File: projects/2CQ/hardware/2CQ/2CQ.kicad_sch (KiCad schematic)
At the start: 1 part

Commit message: KiCad Schematic
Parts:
- added DS1: ~, 128x64_0.96_Disp_Module:128x64_0.96_Disp_Module, symbol 2CQ:SSD1306_0.96_128x64_7P
- added EP1: EURORACK_POWERHEADER, symbol ES_Daisy_Patch_SM_FB_Rev1-eagle-import:EURORACK_POWERHEADER
- added J_CV1, J_CV2, J_CV3, J_CV4, J_CV5, J_CV6, J_CV7, J_CV8: EURO_JACK, symbol ES_Daisy_Patch_SM_FB_Rev1-eagle-import:EURO_JACK
- added S1: TAC_SWITCH_PTH, symbol ES_Daisy_Patch_SM_FB_Rev1-eagle-import:TAC_SWITCH_PTH
- added SW1: TOGGLE_ON-ON, symbol ES_Daisy_Patch_SM_FB_Rev1-eagle-import:TOGGLE_ON-ON
- added VR1, VR2, VR3, VR4: M-10K-B-D, ES_Daisy_Patch_SM_FB_Rev1:9MM_SNAP-IN_POT_SILK, symbol ES_Daisy_Patch_SM_FB_Rev1-cache:ES_Daisy_Patch_SM_FB_Rev1-eagle-import_POT_9MM_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
- U1: renamed from 1; footprint (none) -> ES_Daisy_Patch_SM_FB_Rev1:ES_DAISY_PATCH_SM_REV1
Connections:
- net -12V: now reaches U1.A1 (-12V)
- net -12V: now also EP1.-12V0 (-12VIN), EP1.-12V1 (-12VIN)
- net +3V3: now reaches U1.A10 (+3V3)
- net +3V3: now also DS1.2 (VCC)
- net SIG_UART_RX: now reaches U1.A2 (UART_RX)
- net SIG_UART_RX: now also DS1.6 (DC)
- net SIG_UART_TX: now reaches U1.A3 (UART_TX)
- net SIG_UART_TX: now also DS1.5 (RES)
- net GND: now reaches U1.A4 (GND), U1.A7 (GND)
- net GND: now also DS1.1 (GND), EP1.GND0 (GND), EP1.GND1 (GND), EP1.GND2 (GND), EP1.GND3 (GND), EP1.GND4 (GND), EP1.GND5 (GND), J_CV1.GND, J_CV2.GND, J_CV3.GND, J_CV4.GND, J_CV7.GND, J_CV8.GND, S1.3, S1.4, SW1.1 (O), VR1.1, VR2.1, VR3.1, VR4.1
- net +12V: now reaches U1.A5 (+12V)
- net +12V: now also EP1.+12V0 (+12VIN), EP1.+12V1 (+12VIN)
- net +5V: now reaches U1.A6 (+5V)
- net +5V: now also VR1.3, VR2.3, VR3.3, VR4.3
- net SIG_GATE_IN_1: now reaches U1.B10 (GATE_IN_1)
- net SIG_GATE_IN_1: now also J_CV5.TIP
- net SIG_GATE_OUT_1: now reaches U1.B5 (GATE_OUT_1)
- net SIG_GATE_OUT_1: now also J_CV7.TIP
- net SIG_GATE_OUT_2: now reaches U1.B6 (GATE_OUT_2)
- net SIG_GATE_OUT_2: now also J_CV8.TIP
- net SIG_SW_1: now reaches U1.B7 (I2C1_SCL)
- net SIG_SW_1: now also S1.1, S1.2
- net SIG_SW_2: now reaches U1.B8 (I2C1_SDA)
- net SIG_SW_2: now also SW1.2 (P)
- net SIG_GATE_IN_2: now reaches U1.B9 (GATE_IN_2)
- net SIG_GATE_IN_2: now also J_CV6.TIP
- net SIG_CVOUT_2: now reaches U1.C1 (CV_OUT_2)
- net SIG_CVOUT_2: now also J_CV4.TIP
- net SIG_CVOUT_1: now reaches U1.C10 (CV_OUT_1)
- net SIG_CVOUT_1: now also J_CV3.TIP
- net SIG_KNOB4: now reaches U1.C2 (CV4)
- net SIG_KNOB4: now also VR4.2
- net SIG_KNOB3: now reaches U1.C3 (CV3)
- net SIG_KNOB3: now also VR3.2
- net SIG_KNOB2: now reaches U1.C4 (CV2)
- net SIG_KNOB2: now also VR2.2
- net SIG_KNOB1: now reaches U1.C5 (CV1)
- net SIG_KNOB1: now also VR1.2
- net SIG_CV1: now reaches U1.C6 (CV5)
- net SIG_CV1: now also J_CV1.TIP
- net SIG_CV2: now reaches U1.C7 (CV6)
- net SIG_CV2: now also J_CV2.TIP
- net SIG_CV3: now reaches U1.C8 (CV7)
- net SIG_CV4: now reaches U1.C9 (CV8)
- net SIG_SPI_NSS: now reaches U1.D1 (SPI_NSS)
- net SIG_SPI_NSS: now also J_CV5.GND
- net SIG_SPI_SCK: now reaches U1.D10 (SPI_SCK)
- net SIG_SPI_SCK: now also DS1.3 (D0)
- net SD_D3: now reaches U1.D2 (SDMMC_D3)
- net SD_D3: now also J_CV6.GND
- net SD_D2: now reaches U1.D3 (SDMMC_D2)
- net SD_D1: now reaches U1.D4 (SDMMC_D1)
- net SD_D0: now reaches U1.D5 (SDMMC_D0)
- net SD_CK: now reaches U1.D6 (SDMMC_CK)
- net SD_CMD: now reaches U1.D7 (SDMMC_CMD)
- net SIG_SPI_MISO: now reaches U1.D8 (SPI_MISO)
- net SIG_SPI_MOSI: now reaches U1.D9 (SPI_MOSI)
- net SIG_SPI_MOSI: now also DS1.4 (D1)

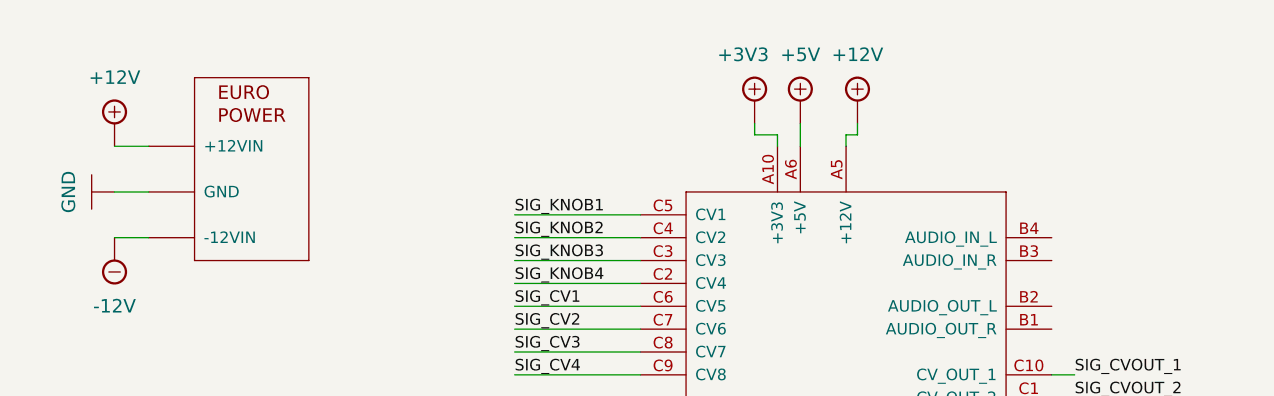
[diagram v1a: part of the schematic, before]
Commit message: Added footprints and some labels
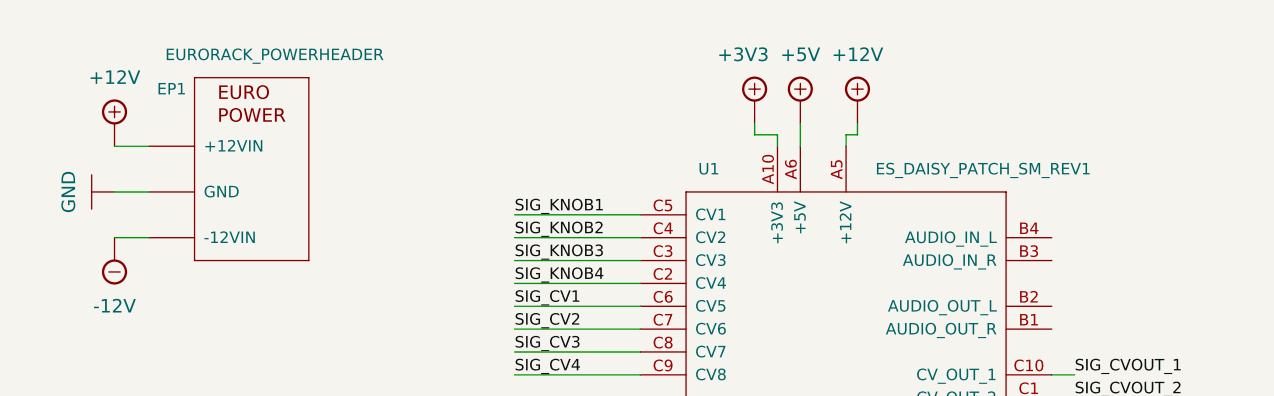
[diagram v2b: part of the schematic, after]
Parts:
- DS1: symbol 2CQ:SSD1306_0.96_128x64_7P -> 2CQ:SSD1306_96_128_64_7P
- EP1: footprint (none) -> ES_Daisy_Patch_SM_FB_Rev1:EURORACK_POWER_SHROUD_LOCK
- J_CV1, J_CV2, J_CV3, J_CV4, J_CV5, J_CV6, J_CV7, J_CV8: footprint (none) -> ES_Daisy_Patch_SM_FB_Rev1:S_JACK
- S1: footprint (none) -> ES_Daisy_Patch_SM_FB_Rev1:TL1105SPF250Q_SILK
- SW1: footprint (none) -> ES_Daisy_Patch_SM_FB_Rev1:TOGGLE_ON-ON
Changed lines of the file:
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@@
   )
   (symbol (lib_id "ES_Daisy_Patch_SM_FB_Rev1-eagle-import:EURORACK_POWERHEADER") (at 36.83 43.18 0) (unit 1)
-    (in_bom yes) (on_board yes) (dnp no) (fields_autoplaced)
-    (property "Reference" "EP1" (at 36.83 43.18 0)
-      (effects (font (size 1.27 1.27)) hide)
-    )
-    (property "Value" "EURORACK_POWERHEADER" (at 36.83 43.18 0)
-      (effects (font (size 1.27 1.27)) hide)
-    )
-    (property "Footprint" "" (at 36.83 43.18 0)
+    (in_bom yes) (on_board yes) (dnp no)
+    (property "Reference" "EP1" (at 29.21 34.29 0)
+      (effects (font (size 1.27 1.27)))
+    )
+    (property "Value" "EURORACK_POWERHEADER" (at 40.64 30.48 0)
+      (effects (font (size 1.27 1.27)))
+    )
+    (property "Footprint" "ES_Daisy_Patch_SM_FB_Rev1:EURORACK_POWER_SHROUD_LOCK" (at 36.83 43.18 0)
       (effects (font (size 1.27 1.27)) hide)
     )
@@
       (effects (font (size 1.4986 1.4986)) (justify left))
     )
-    (property "Footprint" "" (at 66.04 167.64 0)
+    (property "Footprint" "ES_Daisy_Patch_SM_FB_Rev1:S_JACK" (at 66.04 167.64 0)
       (effects (font (size 1.27 1.27)) hide)
     )
@@
       (effects (font (size 1.4986 1.4986)) (justify left))
     )
-    (property "Footprint" "" (at 63.5 124.46 0)
+    (property "Footprint" "ES_Daisy_Patch_SM_FB_Rev1:S_JACK" (at 63.5 124.46 0)
       (effects (font (size 1.27 1.27)) hide)
     )
@@
       (effects (font (size 1.4986 1.4986)))
     )
-    (property "Footprint" "" (at 231.14 90.17 0)
+    (property "Footprint" "ES_Daisy_Patch_SM_FB_Rev1:TOGGLE_ON-ON" (at 231.14 90.17 0)
       (effects (font (size 1.27 1.27)) hide)
     )
@@
       (effects (font (size 1.4986 1.4986)) (justify left))
     )
-    (property "Footprint" "" (at 30.48 124.46 0)
+    (property "Footprint" "ES_Daisy_Patch_SM_FB_Rev1:S_JACK" (at 30.48 124.46 0)
       (effects (font (size 1.27 1.27)) hide)
     )
@@
   )
   (symbol (lib_id "ES_Daisy_Patch_SM_FB_Rev1-eagle-import:ES_DAISY_PATCH_SM_REV1") (at 104.14 73.66 0) (unit 1)
-    (in_bom yes) (on_board yes) (dnp no) (fields_autoplaced)
-    (property "Reference" "U1" (at 104.14 73.66 0)
-      (effects (font (size 1.27 1.27)) hide)
-    )
-    (property "Value" "ES_DAISY_PATCH_SM_REV1" (at 104.14 73.66 0)
-      (effects (font (size 1.27 1.27)) hide)
+    (in_bom yes) (on_board yes) (dnp no)
+    (property "Reference" "U1" (at 88.9 43.18 0)
+      (effects (font (size 1.27 1.27)))
+    )
+    (property "Value" "ES_DAISY_PATCH_SM_REV1" (at 119.38 43.18 0)
+      (effects (font (size 1.27 1.27)))
     )
     (property "Footprint" "ES_Daisy_Patch_SM_FB_Rev1:ES_DAISY_PATCH_SM_REV1" (at 104.14 73.66 0)
@@
       (effects (font (size 1.4986 1.4986)) (justify left))
     )
-    (property "Footprint" "" (at 30.48 144.78 0)
+    (property "Footprint" "ES_Daisy_Patch_SM_FB_Rev1:S_JACK" (at 30.48 144.78 0)
       (effects (font (size 1.27 1.27)) hide)
     )
@@
       (effects (font (size 1.4986 1.4986)) (justify left))
     )
-    (property "Footprint" "" (at 63.5 144.78 0)
+    (property "Footprint" "ES_Daisy_Patch_SM_FB_Rev1:S_JACK" (at 63.5 144.78 0)
       (effects (font (size 1.27 1.27)) hide)
     )
@@
     )
   )
-  (symbol (lib_id "2CQ:SSD1306_0.96_128x64_7P") (at 36.83 78.74 270) (unit 1)
+  (symbol (lib_id "2CQ:SSD1306_96_128_64_7P") (at 36.83 78.74 270) (unit 1)
     (in_bom yes) (on_board yes) (dnp no) (fields_autoplaced)
     (property "Reference" "DS1" (at 26.67 77.47 90)
@@
       (effects (font (size 1.4986 1.4986)) (justify left))
     )
-    (property "Footprint" "" (at 64.77 185.42 0)
+    (property "Footprint" "ES_Daisy_Patch_SM_FB_Rev1:S_JACK" (at 64.77 185.42 0)
       (effects (font (size 1.27 1.27)) hide)
     )
@@
     )
   )
-  (symbol (lib_id "ES_Daisy_Patch_SM_FB_Rev1-eagle-import:EURO_JACK") (at 30.48 166.37 0) (mirror y) (unit 1)
+  (symbol (lib_name "EURO_JACK_1") (lib_id "ES_Daisy_Patch_SM_FB_Rev1-eagle-import:EURO_JACK") (at 30.48 166.37 0) (mirror y) (unit 1)
     (in_bom yes) (on_board yes) (dnp no)
     (property "Reference" "J_CV5" (at 31.75 161.29 0)
@@
       (effects (font (size 1.4986 1.4986)) (justify left))
     )
-    (property "Footprint" "" (at 30.48 166.37 0)
+    (property "Footprint" "ES_Daisy_Patch_SM_FB_Rev1:S_JACK" (at 30.48 166.37 0)
       (effects (font (size 1.27 1.27)) hide)
     )
@@
       (effects (font (size 1.4986 1.4986)) (justify left))
     )
-    (property "Footprint" "" (at 29.21 184.15 0)
+    (property "Footprint" "ES_Daisy_Patch_SM_FB_Rev1:S_JACK" (at 29.21 184.15 0)
       (effects (font (size 1.27 1.27)) hide)
     )
@@
       (effects (font (size 1.4986 1.4986)))
     )
-    (property "Footprint" "" (at 187.96 90.17 0)
-      (effects (font (size 1.27 1.27)) hide)
-    )
+    (property "Footprint" "ES_Daisy_Patch_SM_FB_Rev1:TL1105SPF250Q_SILK" (at 187.96 90.17 0)
+      (effects (font (size 1.27 1.27)) hide)
+    )

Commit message: Use project footprint for 128x64_0.96_Disp_Module
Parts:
- DS1: footprint 128x64_0.96_Disp_Module:128x64_0.96_Disp_Module -> 2CQ:128x64_0.96_Disp_Module
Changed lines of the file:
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@@
       (effects (font (size 1.27 1.27)))
     )
-    (property "Footprint" "128x64_0.96_Disp_Module:128x64_0.96_Disp_Module" (at 36.83 78.74 0)
+    (property "Footprint" "2CQ:128x64_0.96_Disp_Module" (at 36.83 78.74 0)
       (effects (font (size 1.27 1.27)) hide)
     )

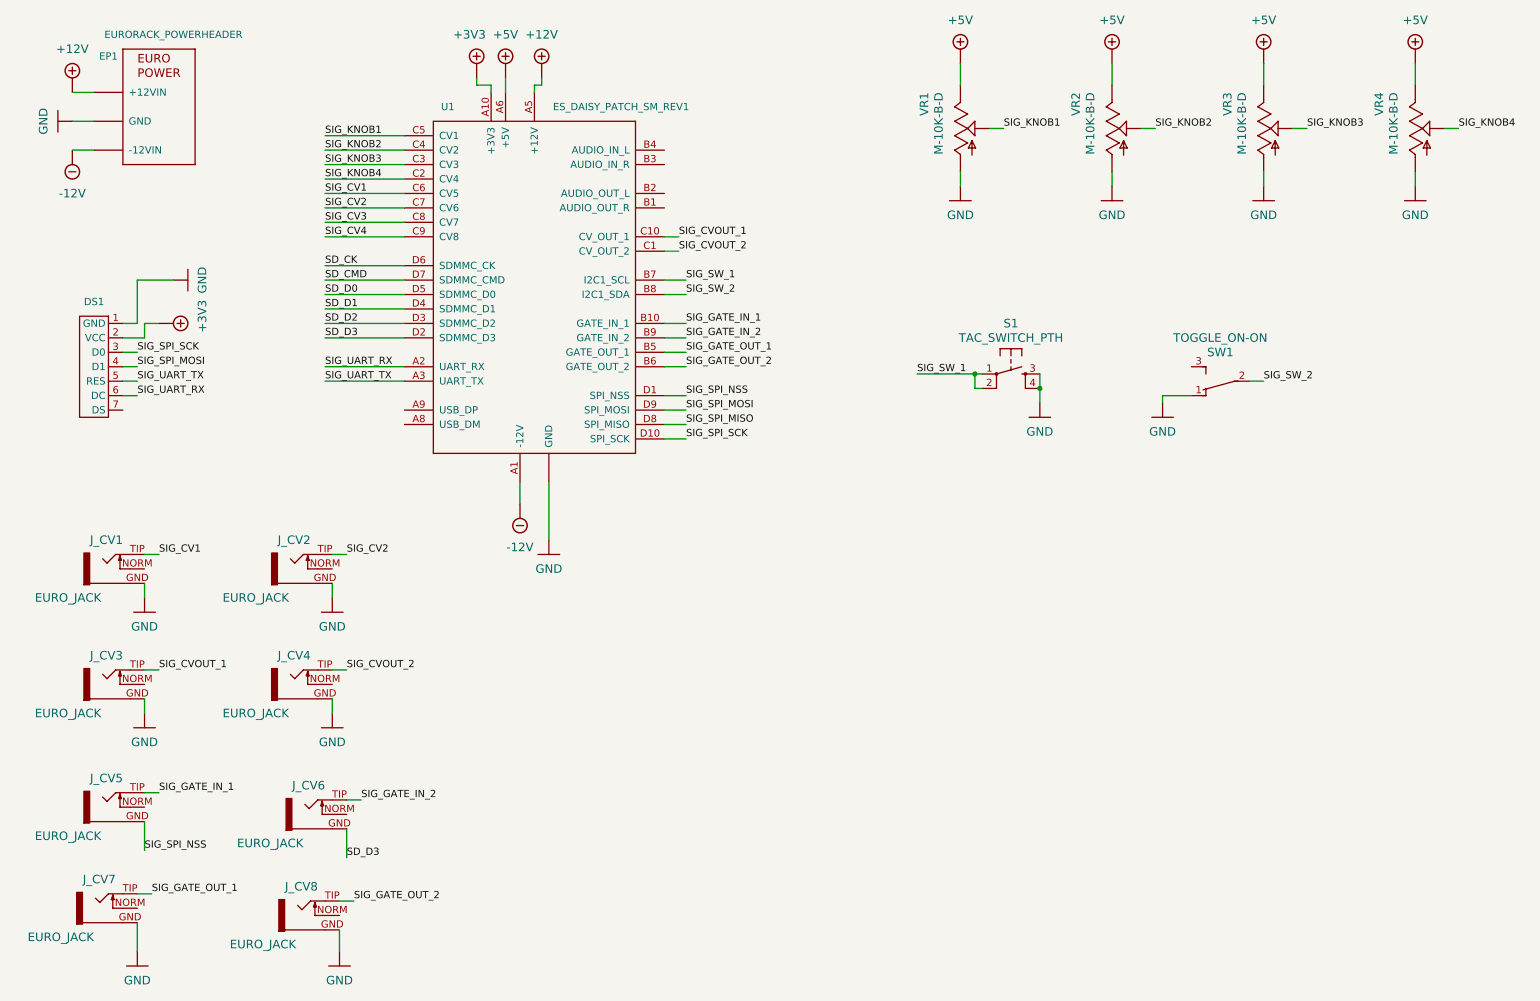
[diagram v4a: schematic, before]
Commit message: A bunch of symbol and footprint optimizations
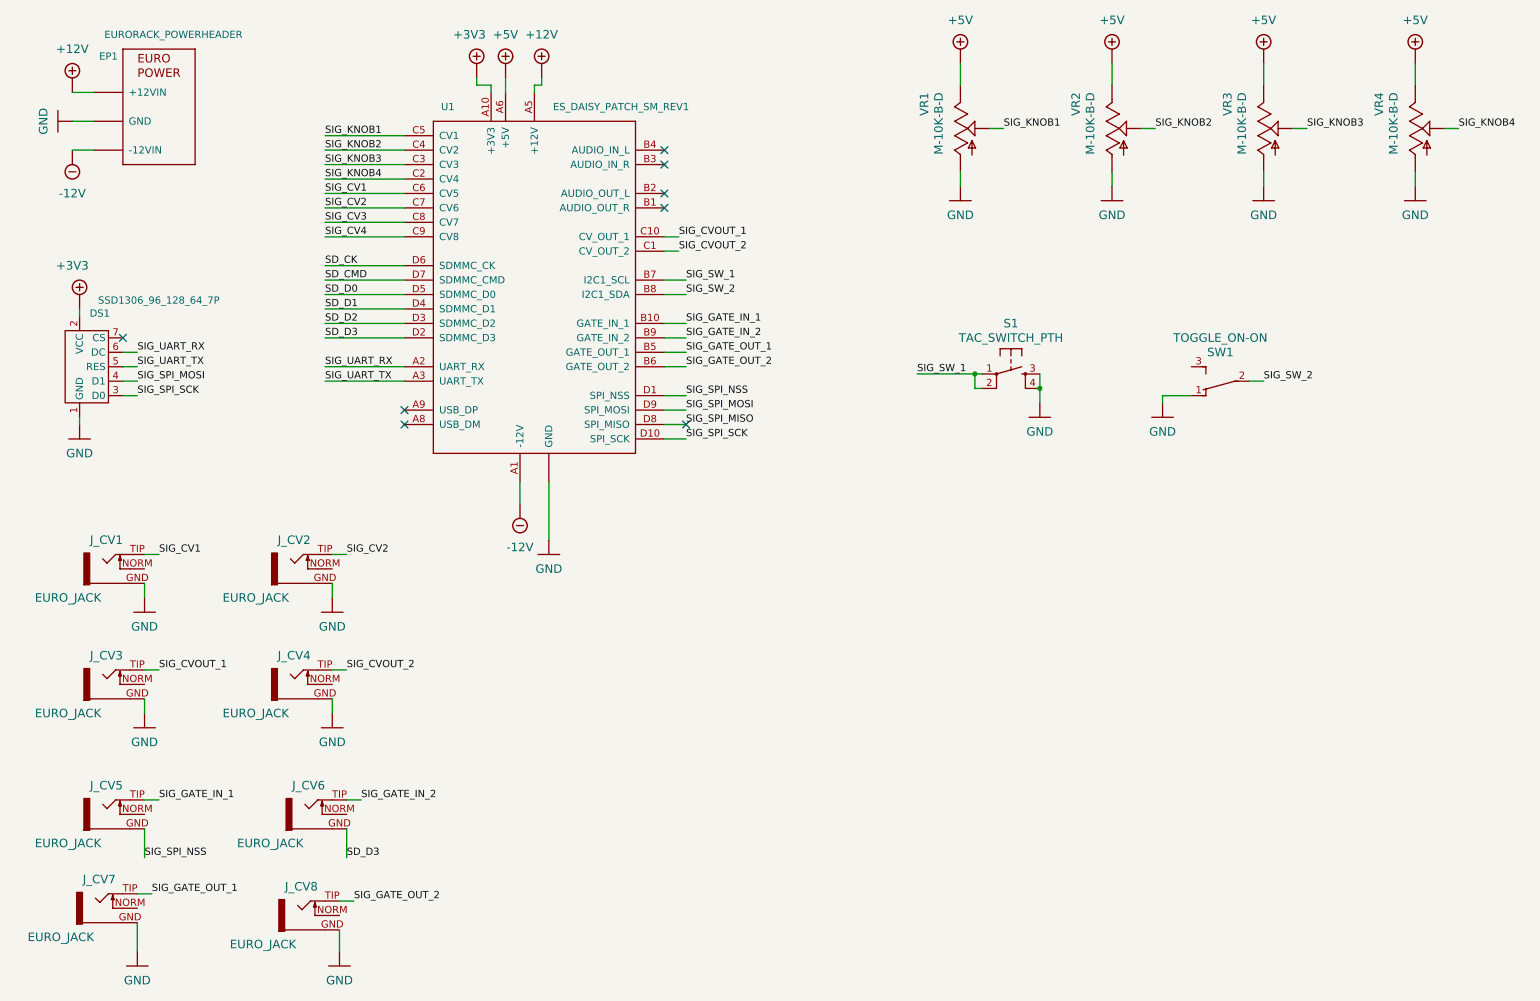
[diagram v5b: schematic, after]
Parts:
- DS1: value ~ -> SSD1306_96_128_64_7P
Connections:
- no-connect marks 0 -> 8
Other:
- moved on the sheet: DS1, J_CV5

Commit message: Some electrical check stuff
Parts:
- VR1, VR2, VR3, VR4: symbol ES_Daisy_Patch_SM_FB_Rev1-cache:ES_Daisy_Patch_SM_FB_Rev1-eagle-import_POT_9MM_SNAP-IN__ -> ES_Daisy_Patch_SM_FB_Rev1-eagle-import:POT_9MM_SNAP-IN_
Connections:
- no-connect marks 8 -> 24
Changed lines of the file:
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@@
+	)
+	(no_connect
+		(at 81.28 81.28)
+	)
+	(no_connect
+		(at 35.56 124.46)
+	)
+	(no_connect
+		(at 81.28 73.66)
+	)
+	(no_connect
+		(at 81.28 71.12)
+	)
+	(no_connect
+		(at 34.29 184.15)
 	)
 	(no_connect
@@
 	)
 	(no_connect
+		(at 71.12 167.64)
+	)
+	(no_connect
 		(at 127 50.8)
+	)
+	(no_connect
+		(at 35.56 167.64)
+	)
+	(no_connect
+		(at 35.56 144.78)
+	)
+	(no_connect
+		(at 69.85 185.42)
 	)
 	(no_connect
@@
 	)
 	(no_connect
+		(at 68.58 124.46)
+	)
+	(no_connect
 		(at 130.81 99.06)
+	)
+	(no_connect
+		(at 81.28 63.5)
+	)
+	(no_connect
+		(at 68.58 144.78)
 	)
 	(no_connect
 		(at 127 58.42)
+	)
+	(no_connect
+		(at 81.28 76.2)
+	)
+	(no_connect
+		(at 81.28 66.04)
+	)
+	(no_connect
+		(at 219.71 88.9)
+	)
+	(no_connect
+		(at 81.28 78.74)
 	)
 	(wire
@@
 	)
 	(symbol
-		(lib_id "ES_Daisy_Patch_SM_FB_Rev1-cache:ES_Daisy_Patch_SM_FB_Rev1-eagle-import_POT_9MM_SNAP-IN__")
+		(lib_id "ES_Daisy_Patch_SM_FB_Rev1-eagle-import:POT_9MM_SNAP-IN_")
 		(at 232.41 46.99 0)
 		(unit 1)
@@
 	)
 	(symbol
-		(lib_id "ES_Daisy_Patch_SM_FB_Rev1-cache:ES_Daisy_Patch_SM_FB_Rev1-eagle-import_POT_9MM_SNAP-IN__")
+		(lib_id "ES_Daisy_Patch_SM_FB_Rev1-eagle-import:POT_9MM_SNAP-IN_")
 		(at 205.74 46.99 0)
 		(unit 1)
@@
 	)
 	(symbol
-		(lib_id "ES_Daisy_Patch_SM_FB_Rev1-cache:ES_Daisy_Patch_SM_FB_Rev1-eagle-import_POT_9MM_SNAP-IN__")
+		(lib_id "ES_Daisy_Patch_SM_FB_Rev1-eagle-import:POT_9MM_SNAP-IN_")
 		(at 259.08 46.99 0)
 		(unit 1)
@@
 	)
 	(symbol
-		(lib_id "ES_Daisy_Patch_SM_FB_Rev1-cache:ES_Daisy_Patch_SM_FB_Rev1-eagle-import_POT_9MM_SNAP-IN__")
+		(lib_id "ES_Daisy_Patch_SM_FB_Rev1-eagle-import:POT_9MM_SNAP-IN_")
 		(at 179.07 46.99 0)
 		(unit 1)
